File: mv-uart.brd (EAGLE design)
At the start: 37.9 x 33.5 mm, 39 parts, among them SW1 DIP_SP6T, U1 IP4234CZ6, U2 CP2105-GM, U3 LDO_SHD_ADJ-AP2127K-ADJ, X1 MINI-USB-SHIELD-UX60-MB-5ST

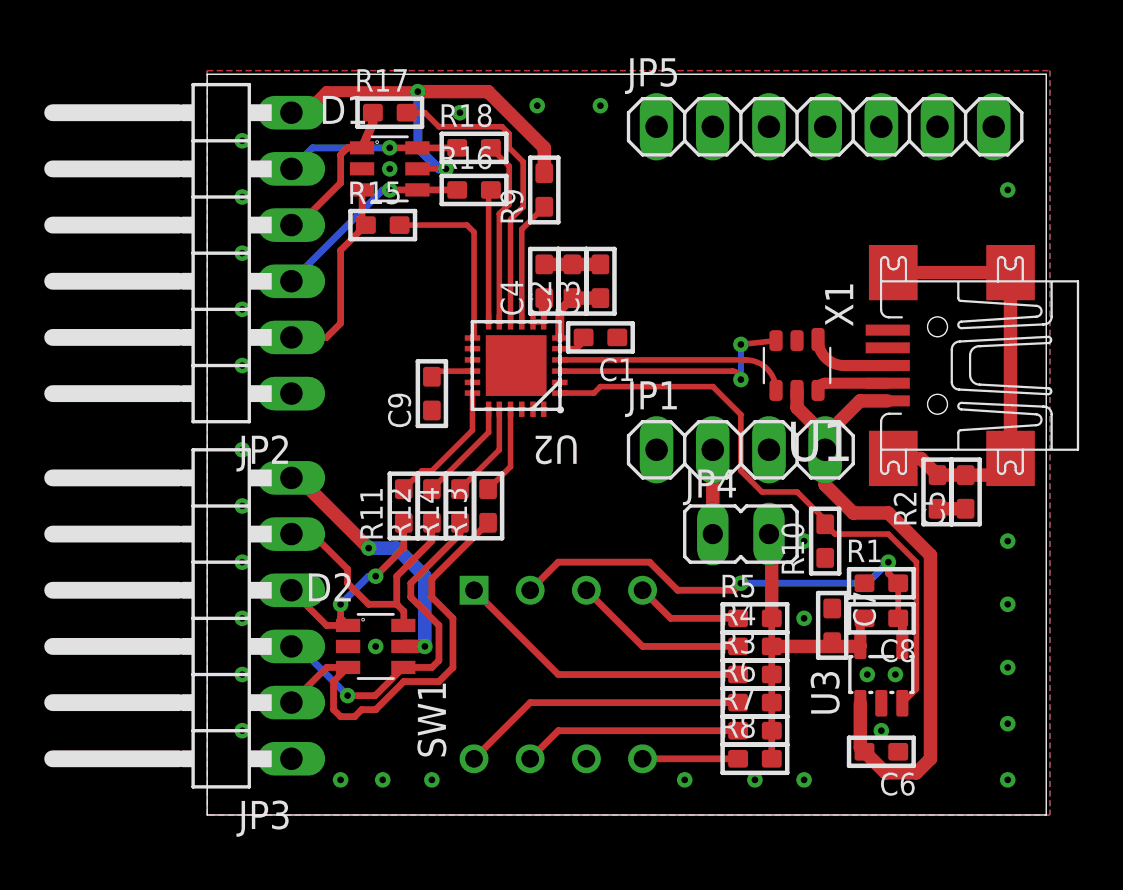
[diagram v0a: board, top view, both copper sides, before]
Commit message: first fully routed version of mv-uart
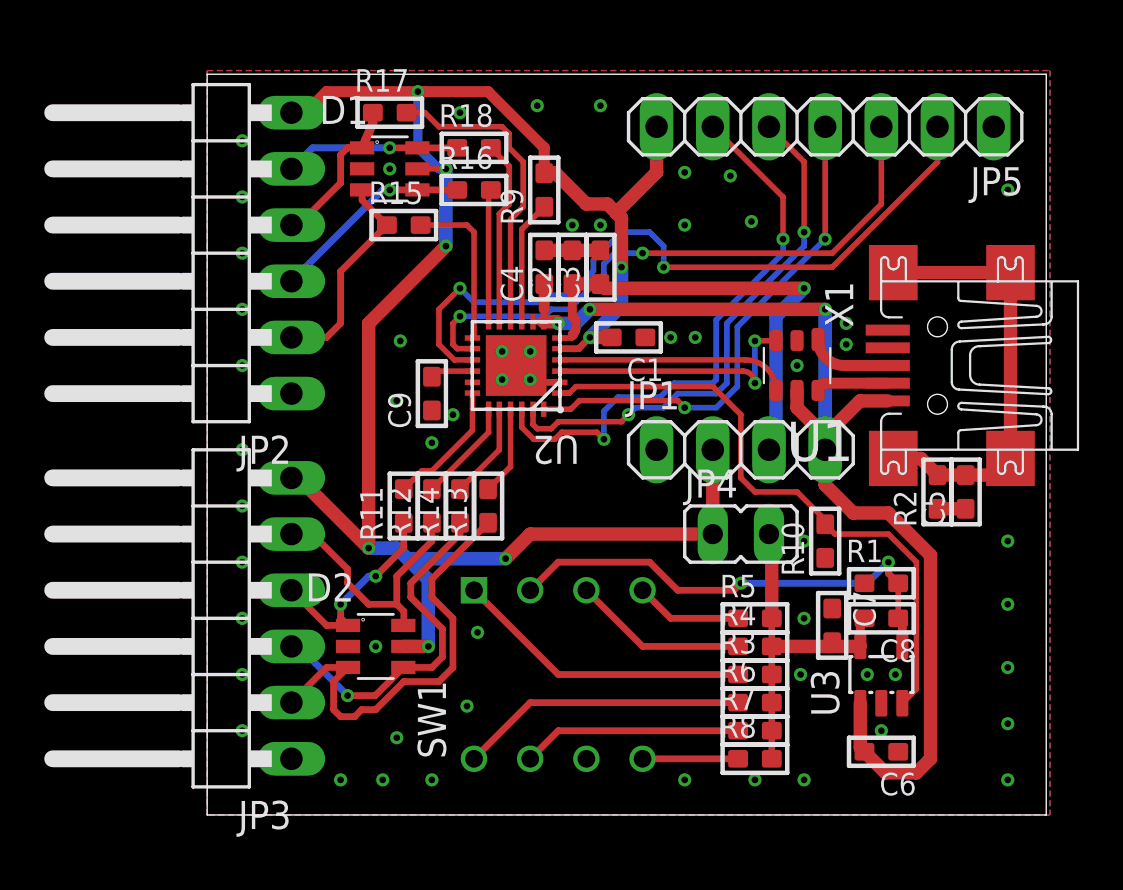
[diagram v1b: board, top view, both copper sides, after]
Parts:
- moved C1 1.27 mm to (19.1, 21.6)
- moved R15 0.95 mm to (8.89, 26.7)
- moved C2 0.64 mm to (16.5, 24.8)
- moved C3 0.64 mm to (17.8, 24.8)
- moved C4 0.64 mm to (15.2, 24.8)
- turned JP5 to 180 degrees
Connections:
- net GND: now also U2.25
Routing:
- net VIO: track 36.9 -> 86.8 mm, vias 4 -> 8
- net GPIO.0_ECI: track 0.00 -> 33.0 mm, vias 0 -> 2
- net GPIO.1_ECI: track 0.00 -> 27.3 mm, vias 0 -> 2
- net GPIO.2_SCI: track 0.00 -> 26.0 mm, vias 0 -> 2
- net GPIO.1_SCI: track 0.00 -> 24.1 mm, vias 0 -> 2
- net GPIO.0_SCI: track 0.00 -> 22.8 mm, vias 0 -> 2
- net USB_VBUS: track 31.0 -> 51.0 mm, vias 0 -> 3
- net VDD_3V45: track 3.31 -> 21.8 mm, vias 0 -> 1
- net GND: track 3.81 -> 6.10 mm, vias 33 -> 56
- net N$14: track 8.31 -> 7.36 mm
- net TXD_ECI: track 9.06 -> 9.85 mm
